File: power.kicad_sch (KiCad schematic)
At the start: 64 parts, among them U801 TPS566231P, U802 TPS566231P, U803 TPS566231P, U804 TPS566231P

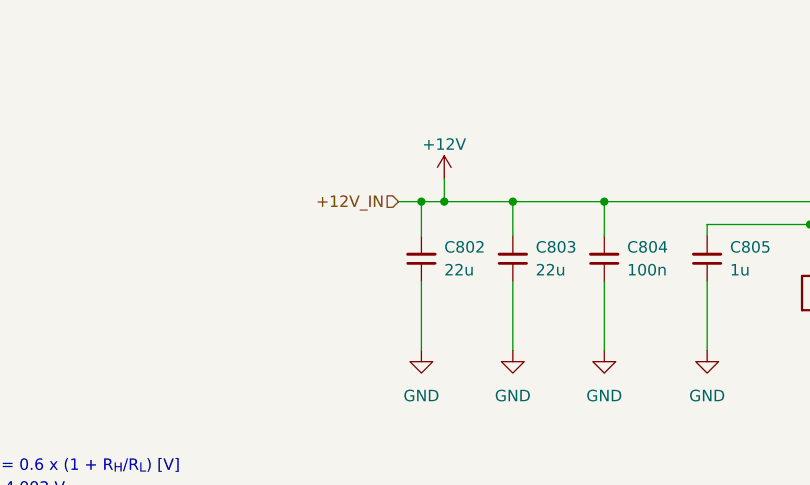
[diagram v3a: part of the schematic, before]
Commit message: [#100282] Clear ERC
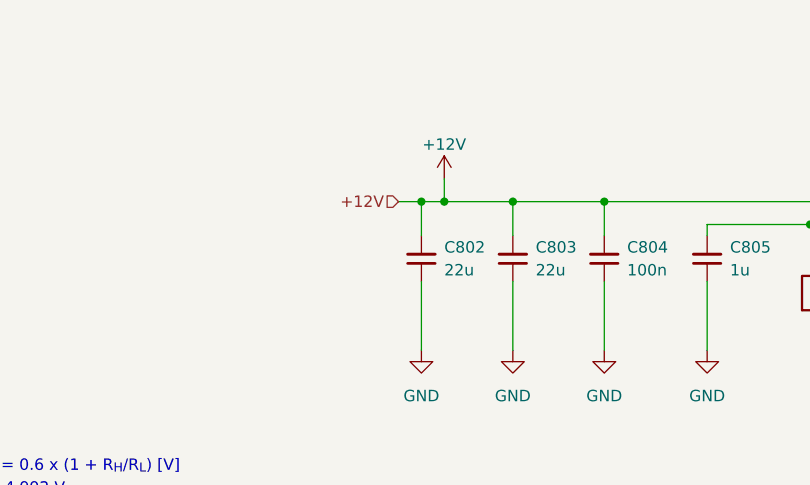
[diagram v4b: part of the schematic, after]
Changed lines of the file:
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@@
 	)
 	(junction
-		(at 130.81 40.64)
-		(diameter 0)
-		(color 0 0 0 0)
-	)
-	(junction
 		(at 128.27 153.67)
 		(diameter 0)
@@
 	)
 	(junction
+		(at 130.81 40.64)
+		(diameter 0)
+		(color 0 0 0 0)
+	)
+	(junction
 		(at 280.67 153.67)
 		(diameter 0)
@@
 	(wire
 		(pts
-			(xy 130.81 38.1) (xy 130.81 40.64)
-		)
-		(stroke
-			(width 0)
-			(type default)
-		)
-	)
-	(wire
-		(pts
 			(xy 260.35 153.67) (xy 270.51 153.67)
 		)
@@
 	(wire
 		(pts
+			(xy 130.81 38.1) (xy 130.81 40.64)
+		)
+		(stroke
+			(width 0)
+			(type default)
+		)
+	)
+	(wire
+		(pts
 			(xy 270.51 162.56) (xy 270.51 170.18)
 		)
@@
 	(wire
 		(pts
-			(xy 130.81 40.64) (xy 138.43 40.64)
+			(xy 125.73 40.64) (xy 138.43 40.64)
 		)
 		(stroke
@@
 	(wire
 		(pts
-			(xy 125.73 40.64) (xy 130.81 40.64)
-		)
-		(stroke
-			(width 0)
-			(type default)
-		)
-	)
-	(wire
-		(pts
 			(xy 138.43 100.33) (xy 148.59 100.33)
 		)
@@
 		)
 	)
-	(hierarchical_label "+12V_IN"
+	(hierarchical_label "+12V"
 		(shape input)
 		(at 125.73 40.64 180)
@@
 	)
 	(symbol
+		(lib_id "antmicropower:+12V")
+		(at 130.81 38.1 0)
+		(unit 1)
+		(body_style 1)
+		(exclude_from_sim no)
+		(in_bom yes)
+		(on_board yes)
+		(in_pos_files yes)
+		(dnp no)
+		(property "Reference" "#PWR0802"
+			(at 130.81 41.91 0)
+			(hide yes)
+			(show_name no)
+			(do_not_autoplace no)
+			(effects
+				(font
+					(size 1.27 1.27)
+				)
+			)
+		)
+		(property "Value" "+12V"
+			(at 130.81 34.29 0)
+			(show_name no)
+			(do_not_autoplace no)
+			(effects
+				(font
+					(size 1.27 1.27)
+				)
+			)
+		)
+		(property "Footprint" ""
+			(at 130.81 38.1 0)
+			(hide yes)
+			(show_name no)
+			(do_not_autoplace no)
+			(effects
+				(font
+					(size 1.27 1.27)
+				)
+			)
+		)
+		(property "Datasheet" ""
+			(at 130.81 38.1 0)
+			(hide yes)
+			(show_name no)
+			(do_not_autoplace no)
+			(effects
+				(font
+					(size 1.27 1.27)
+				)
+			)
+		)
+		(property "Description" ""
+			(at 130.81 44.45 0)
+			(hide yes)
+			(show_name no)
+			(do_not_autoplace no)
+			(effects
+				(font
+					(size 1.27 1.27)
+				)
+				(justify left bottom)
+			)
+		)
+		(pin "1"
+		)
+		(instances
+			(project "altera-modular-agilex-5-dc-scm"
+				(path "/6bb9d978-a328-4b30-874b-55170a976185/ec2bc394-f073-4549-a45a-609fd3c852aa"
+					(reference "#PWR0802")
+					(unit 1)
+				)
+			)
+		)
+	)
+	(symbol
 		(lib_id "antmicroResistors0402:R_100k_0402")
 		(at 171.45 166.37 90)
@@
 					(unit 1)
 				)
-			)
-		)
-	)
-	(symbol
-		(lib_id "antmicropower:+12V")
-		(at 130.81 38.1 0)
-		(unit 1)
-		(body_style 1)
-		(exclude_from_sim no)
-		(in_bom yes)
-		(on_board yes)
-		(in_pos_files yes)
-		(dnp no)
-		(property "Reference" "#PWR0802"
-			(at 130.81 41.91 0)
-			(hide yes)
-			(show_name no)
-			(do_not_autoplace no)
-			(effects
-				(font
-					(size 1.27 1.27)
-				)
-			)
-		)
-		(property "Value" "+12V"
-			(at 130.81 34.29 0)
-			(show_name no)
-			(do_not_autoplace no)
-			(effects
-				(font
-					(size 1.27 1.27)
-				)
-			)
-		)
-		(property "Footprint" ""
-			(at 130.81 38.1 0)
-			(hide yes)
-			(show_name no)
-			(do_not_autoplace no)
-			(effects
-				(font
-					(size 1.27 1.27)
-				)
-			)
-		)
-		(property "Datasheet" ""
-			(at 130.81 38.1 0)
-			(hide yes)
-			(show_name no)
-			(do_not_autoplace no)
-			(effects
-				(font
-					(size 1.27 1.27)
-				)
-			)
-		)
-		(property "Description" ""
-			(at 130.81 44.45 0)
-			(hide yes)
-			(show_name no)
-			(do_not_autoplace no)
-			(effects
-				(font
-					(size 1.27 1.27)
-				)
-				(justify left bottom)
-			)
-		)
-		(pin "1"
-		)
-		(instances
-			(project "altera-modular-agilex-5-dc-scm"
-				(path "/6bb9d978-a328-4b30-874b-55170a976185/ec2bc394-f073-4549-a45a-609fd3c852aa"
-					(reference "#PWR0802")
-					(unit 1)
-				)

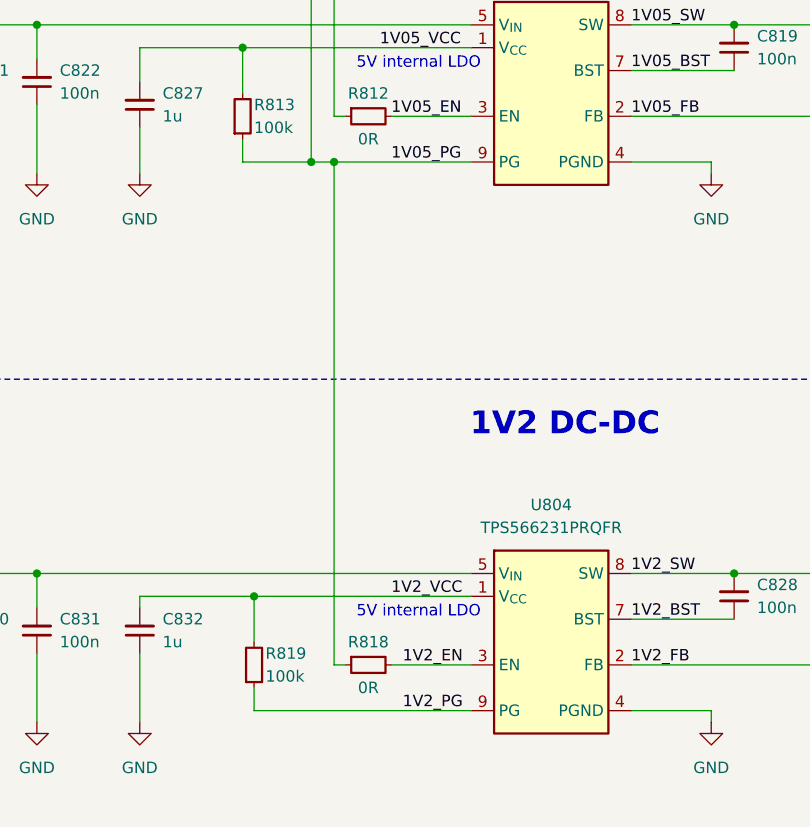
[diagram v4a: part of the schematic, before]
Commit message: [#99852] Add PONRST control to USB controller
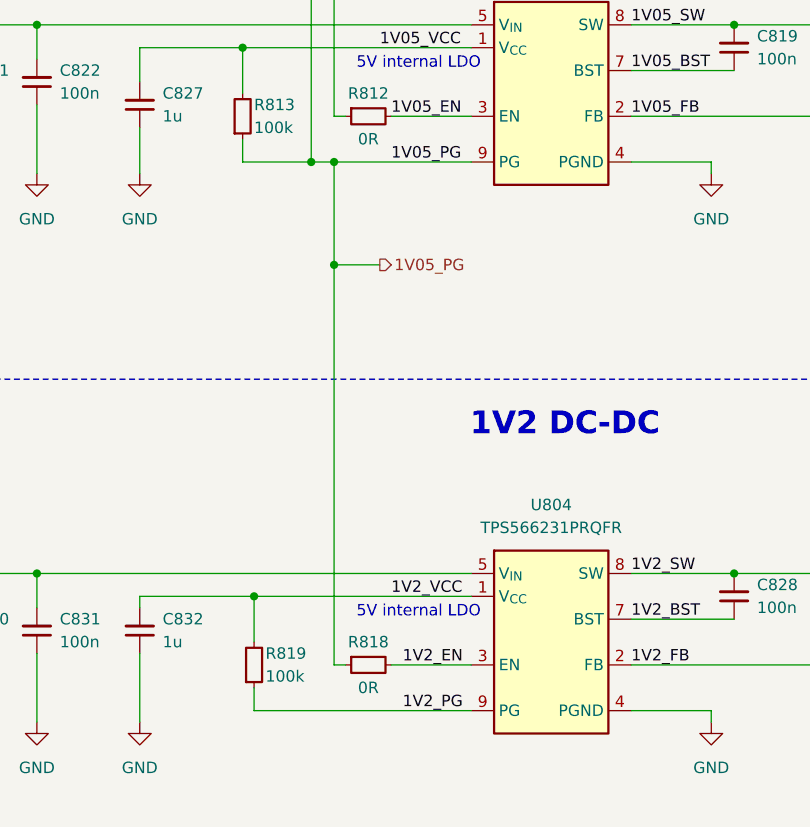
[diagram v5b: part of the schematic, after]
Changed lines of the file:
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@@
+	)
+	(junction
+		(at 181.61 180.34)
+		(diameter 0)
+		(color 0 0 0 0)
 	)
 	(junction
@@
 	(wire
 		(pts
+			(xy 181.61 180.34) (xy 181.61 224.79)
+		)
+		(stroke
+			(width 0)
+			(type default)
+		)
+	)
+	(wire
+		(pts
 			(xy 243.84 100.33) (xy 243.84 104.14)
 		)
@@
 	(wire
 		(pts
-			(xy 181.61 168.91) (xy 181.61 224.79)
+			(xy 181.61 168.91) (xy 181.61 180.34)
 		)
 		(stroke
@@
 		(pts
 			(xy 138.43 157.48) (xy 138.43 153.67)
+		)
+		(stroke
+			(width 0)
+			(type default)
+		)
+	)
+	(wire
+		(pts
+			(xy 181.61 180.34) (xy 186.69 180.34)
 		)
 		(stroke
@@
 		(effects
 			(font
+				(size 1.27 1.27)
+			)
+			(justify left)
+		)
+	)
+	(hierarchical_label "1V05_PG"
+		(shape output)
+		(at 186.69 180.34 0)
+		(effects
+			(font
